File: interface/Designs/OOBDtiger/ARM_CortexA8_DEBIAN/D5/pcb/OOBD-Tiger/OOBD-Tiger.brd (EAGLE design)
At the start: 63.4 x 38.2 mm, 116 parts, among them IC1 ADM3053M, IC2 ADM3053M, IC4 DS3231, U1 SY6280, U10 MP1482DS, U2 SN65HVD230(SO8), U3 SY6280, U6 SN65HVD230(SO8)

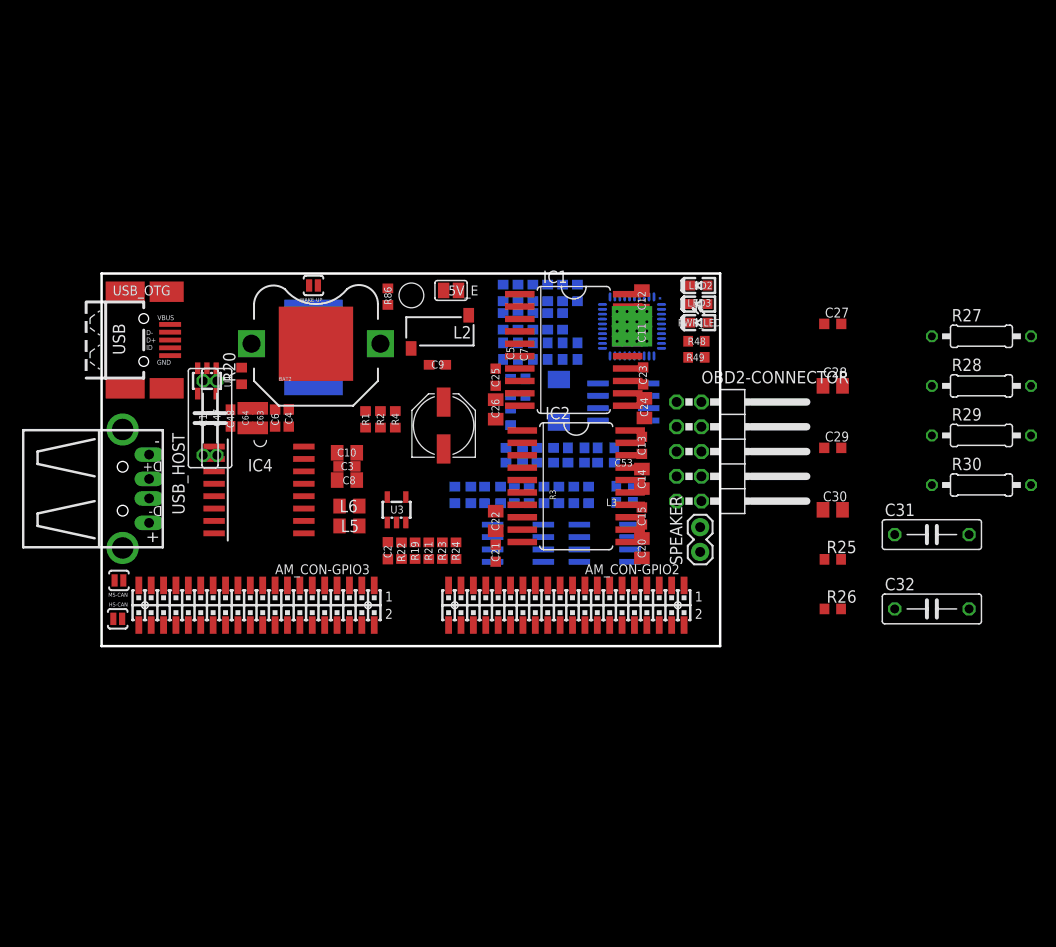
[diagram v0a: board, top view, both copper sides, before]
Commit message: start rearranging the position of the components
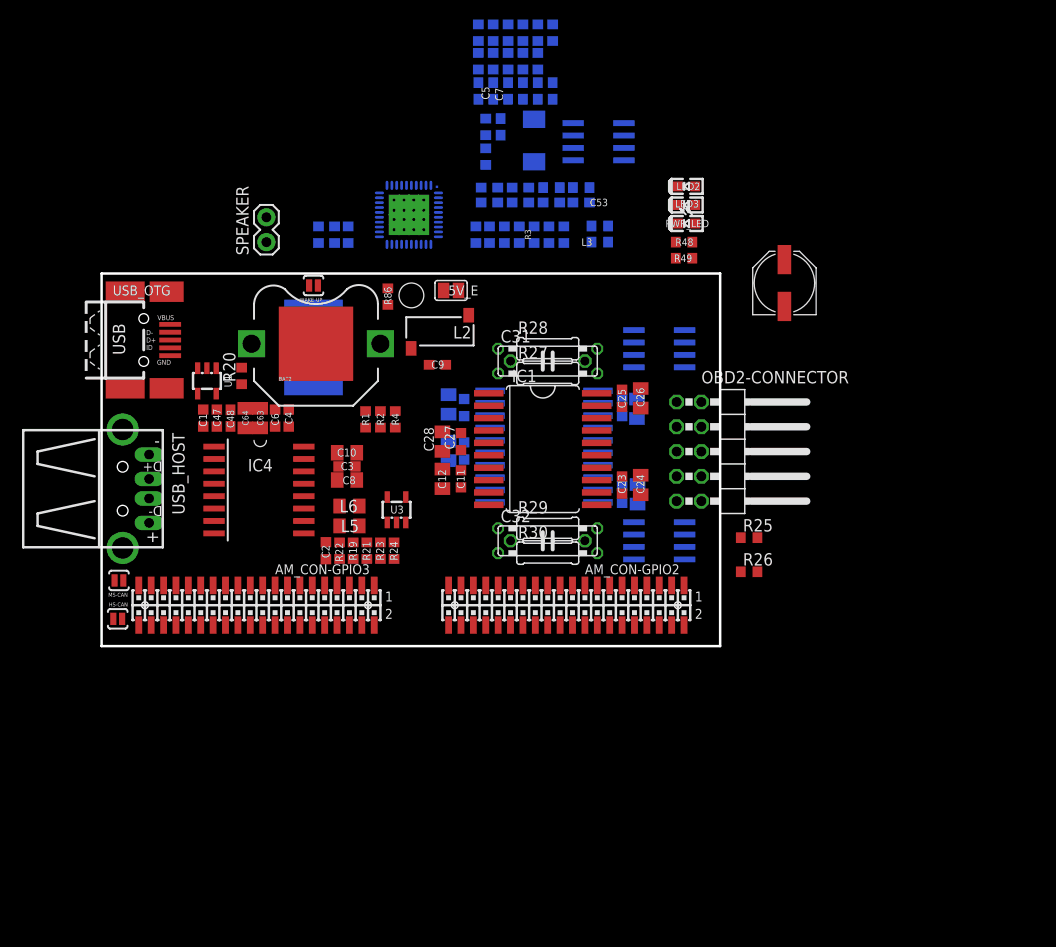
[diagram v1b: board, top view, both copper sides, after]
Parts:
- C1, C47: device rcl:C075-032X103 -> rcl:C0603K
- moved SPEAKER 54.6 mm to (16.9, 41.4)
- moved R29 45.5 mm to (45.7, 12.1)
- moved R30 45.0 mm to (45.7, 9.53)
- moved R27 44.6 mm to (45.7, 27.9)
- moved R28 44.6 mm to (45.7, 30.5)
- moved C31 43.2 mm to (45.7, 29.2)
- moved C28 40.4 mm to (34.9, 21.0), turned to 90 degrees
- moved C32 40.0 mm to (45.7, 10.8)
- moved C27 40.0 mm to (36.8, 21.0), turned to 90 degrees
- moved C30 39.8 mm to (35.6, 20.0), flipped to the bottom, turned to 270 degrees
- moved C51 37.9 mm to (70.0, 37.2)
- moved C29 37.8 mm to (37.1, 20.0), flipped to the bottom, turned to 270 degrees
- moved R5 30.1 mm to (22.2, 42.2)
- moved R6 30.1 mm to (25.3, 42.2)
- moved R7 30.1 mm to (23.9, 42.2)
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
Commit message: add latest modifications to OOBD schematics
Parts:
- removed MS-CAN: OPEN, SparkFun:SJ_2S-NO
- removed R42: 120R, rcl:R0603
- added C33, C34: NA(10nF), resistor:C0603
- added D1, D2: PESD1CAN, Industrialberry:SOT23
- added HS-CAN1: OPEN, SparkFun:SJ_2S-NO
- added R31, R32, R33: 60R, resistor:R0603
- R6: value 120R -> 60R; device rcl:R0603 -> resistor:R0603
- moved R6 67.5 mm to (-6.99, -17.1), flipped to the top, turned to 0 degrees
- flipped U2 to the top, turned to 270 degrees
- flipped U6 to the top, turned to 270 degrees
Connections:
- new net N$30: HS-CAN.1, R32.2
- new net N$32: HS-CAN1.1, R33.2
- net CAN0_H: now also D1.2, R6.2; no longer R42.2
- net CAN0_L: now also D1.1, HS-CAN1.2; no longer MS-CAN.1
- net CAN1_H: now also D2.2, R31.2; no longer R6.2
- net CAN1_L: now also D2.1, HS-CAN.2; no longer HS-CAN.1
- net GND: now also C33.2, C34.2, D1.3, D2.3
- net N$10: now also C34.1, R33.1, R6.1; no longer MS-CAN.2, R42.1
- net N$2: now also C33.1, R31.1, R32.1; no longer HS-CAN.2, R6.1

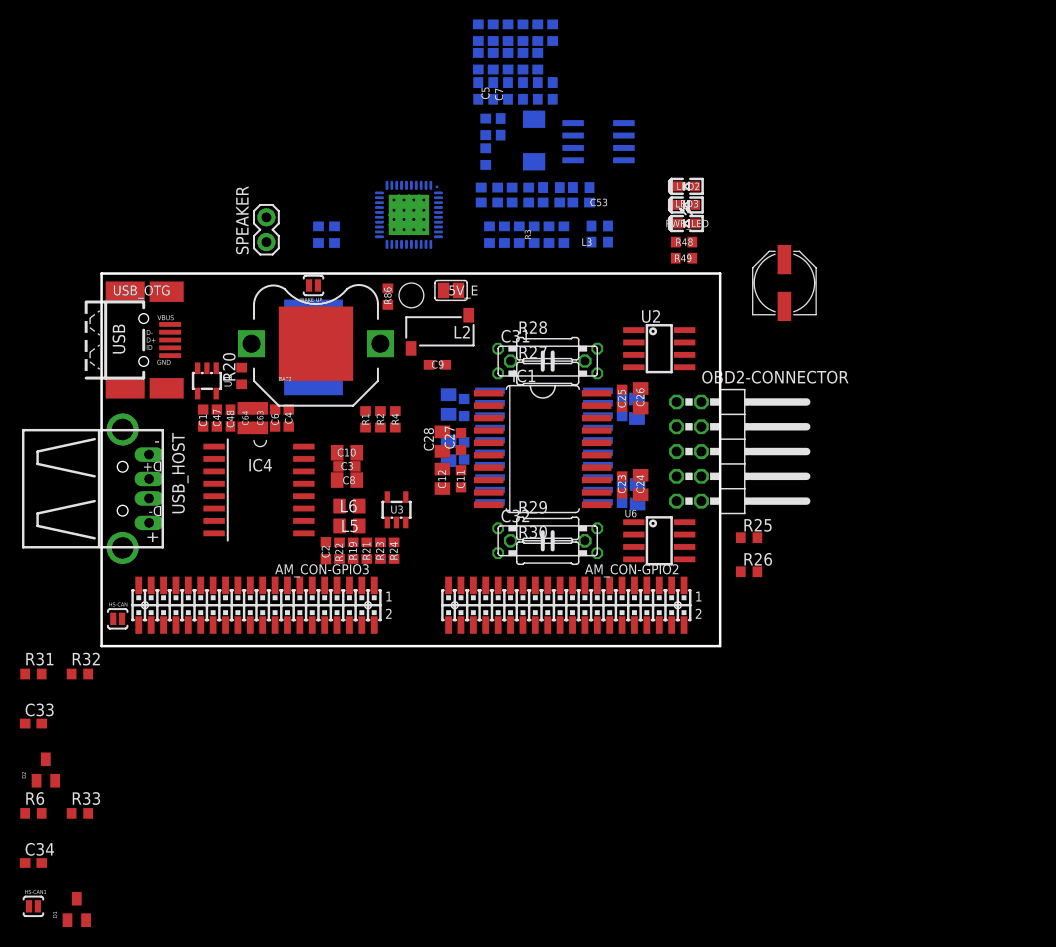
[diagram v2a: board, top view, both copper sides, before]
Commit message: add OOBDpiCAN connector
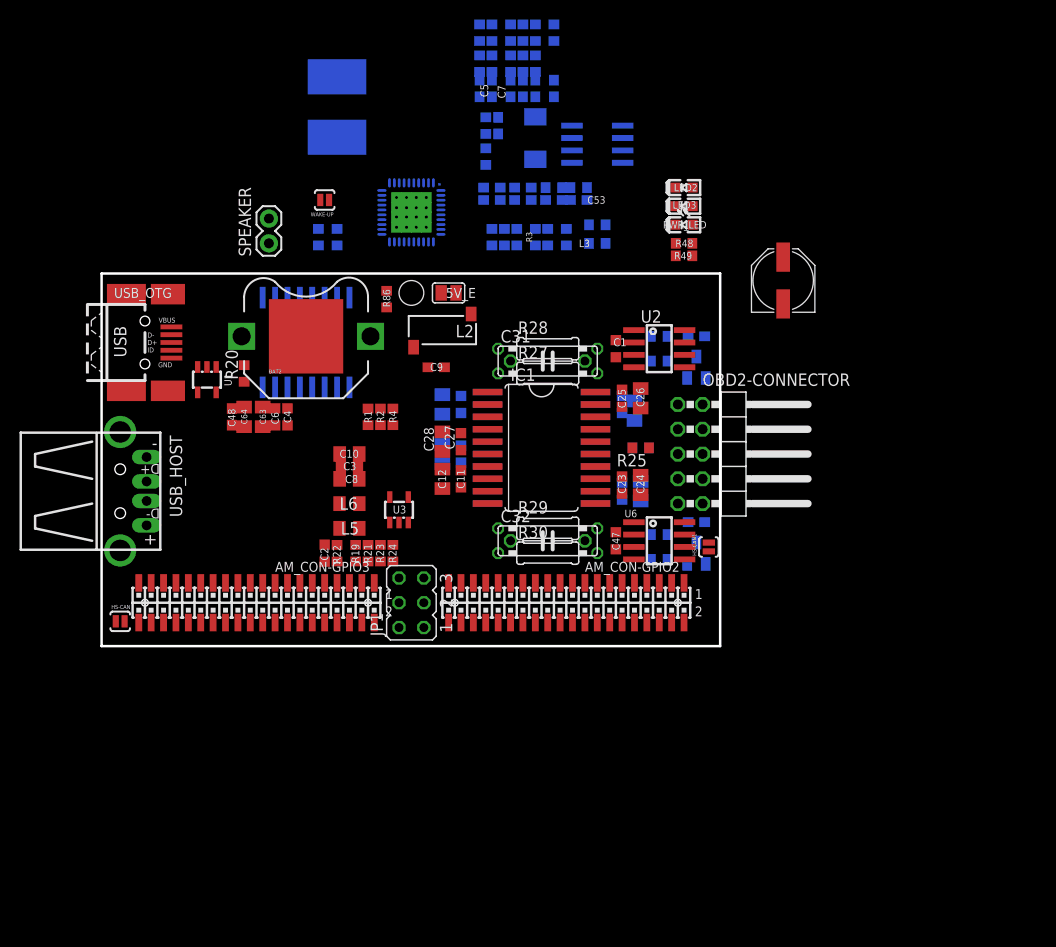
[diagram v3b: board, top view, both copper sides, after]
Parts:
- added JP1: (no value), jumper:JP3Q
- moved C33 78.7 mm to (61.0, 31.8), flipped to the bottom, turned to 180 degrees
- moved D2 78.4 mm to (61.0, 28.6), flipped to the bottom
- moved HS-CAN1 78.4 mm to (62.2, 10.2), turned to 90 degrees
- moved C34 76.4 mm to (61.0, 12.7), flipped to the bottom, turned to 180 degrees
- moved D1 73.2 mm to (61.0, 9.53), flipped to the bottom
- moved R31 72.9 mm to (57.1, 31.8), flipped to the bottom
- moved R6 70.2 mm to (57.1, 11.4), flipped to the bottom
- moved R32 67.5 mm to (57.1, 29.2), flipped to the bottom
- moved R33 64.8 mm to (57.1, 8.89), flipped to the bottom
- moved C1 42.9 mm to (52.7, 30.5), turned to 90 degrees
- moved C47 42.8 mm to (52.7, 10.8), turned to 90 degrees
- moved L11 24.8 mm to (24.1, 55.2)
- moved R26 16.9 mm to (55.2, 20.3), flipped to the bottom, turned to 180 degrees
- moved IC4 15.9 mm to (21.0, 31.1), flipped to the bottom, turned to 180 degrees
- moved R25 14.4 mm to (55.2, 20.3), turned to 180 degrees
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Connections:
- net +5V: now also JP1.1
- net GND: now also JP1.5
- net USB1_DM: now also JP1.2
- net USB1_DP: now also JP1.4

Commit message: Platzierung abgeschlossen, Anschluss LED3 und Bauteilwert L2 offen
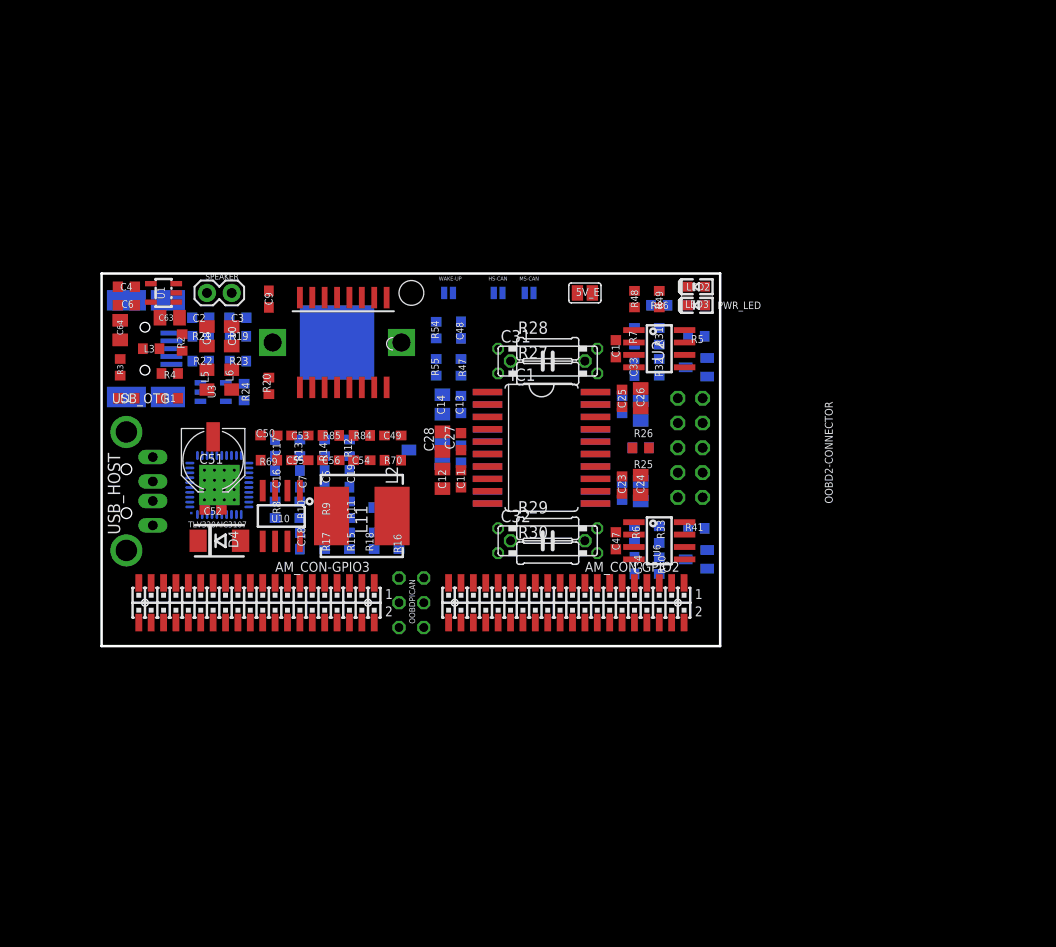
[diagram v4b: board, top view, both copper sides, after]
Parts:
- removed HS-CAN1: OPEN, SparkFun:SJ_2S-NO
- removed OBD2-CONNECTOR: (no value), pinhead:2X05/90
- added MS-CAN: OPEN, SparkFun:SJ_2S-NO
- added OOBD2-CONNECTOR: In-Car Diagnostic, pinhead:2X05/90
- BAT2: value (none) -> 3,6V
- OOBDPICAN: value (none) -> Bridge to PICAN
- TLV320AIC3107: value (none) -> Audio-Amplifier
- moved C51 61.3 mm to (11.4, 19.1), turned to 270 degrees
- moved R17 55.9 mm to (22.9, 10.8), turned to 270 degrees
- moved R15 54.6 mm to (25.4, 10.8), turned to 270 degrees
- moved R18 53.4 mm to (27.9, 10.8), turned to 270 degrees
- moved R16 52.7 mm to (30.5, 10.8), turned to 90 degrees
- moved D4 52.5 mm to (12.1, 10.8), flipped to the top, turned to 0 degrees
- moved R8 52.3 mm to (17.8, 14.0), turned to 270 degrees
- moved C18 52.3 mm to (20.3, 10.8), turned to 270 degrees
- moved L1 51.4 mm to (2.54, 25.4), flipped to the top, turned to 180 degrees
- moved HS-CAN 51.3 mm to (40.6, 36.2), flipped to the bottom
- moved R10 50.6 mm to (20.3, 14.0), turned to 270 degrees
- moved U10 50.0 mm to (18.4, 13.3), flipped to the top, turned to 180 degrees
- moved R13 49.9 mm to (20.3, 20.3), turned to 90 degrees
- moved C52 49.0 mm to (11.4, 14.0), flipped to the top, turned to 180 degrees
- moved R9 48.8 mm to (22.9, 14.0), turned to 270 degrees
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- renumbered JP1 to OOBDPICAN
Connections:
- removed net PMIC_POWER_EN: AM3352-SOM-EVB-PLATFORM.3-18
- net +12V: now also OOBD2-CONNECTOR.10; no longer OBD2-CONNECTOR.10
- net CAN0_H: now also OOBD2-CONNECTOR.1; no longer OBD2-CONNECTOR.1
- net CAN0_L: now also MS-CAN.2, OOBD2-CONNECTOR.2; no longer HS-CAN1.2, OBD2-CONNECTOR.2
- net CAN1_H: now also OOBD2-CONNECTOR.7; no longer OBD2-CONNECTOR.7
- net CAN1_L: now also OOBD2-CONNECTOR.6; no longer OBD2-CONNECTOR.6
- net GND: now also OOBD2-CONNECTOR.3; no longer OBD2-CONNECTOR.3
- net N$32: now also MS-CAN.1; no longer HS-CAN1.1
- net P3_20/LED2: now also AM3352-SOM-EVB-PLATFORM.4-23
